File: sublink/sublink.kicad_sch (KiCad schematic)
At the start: 44 parts, among them J1 ZL315-4SGH, Q1 YJL2305A, SW1 SW_Push, SW2 SW_Push, SW3 SW_Push, U1 ATtiny414-SS, U2 OKY3402, U3 JS202011

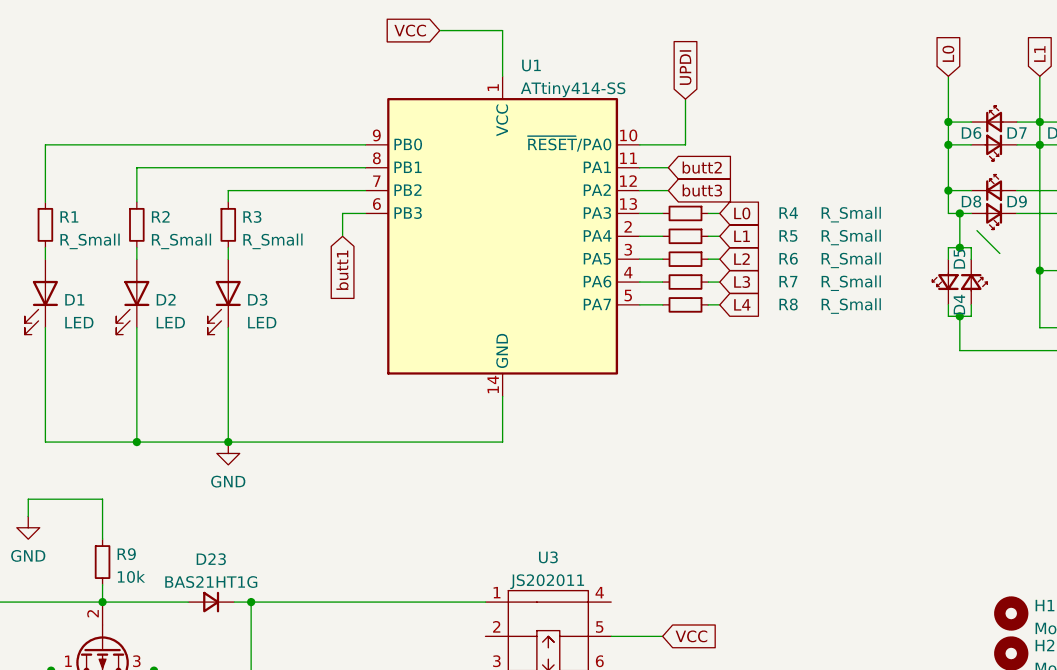
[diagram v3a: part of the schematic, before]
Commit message: first pass all components placement
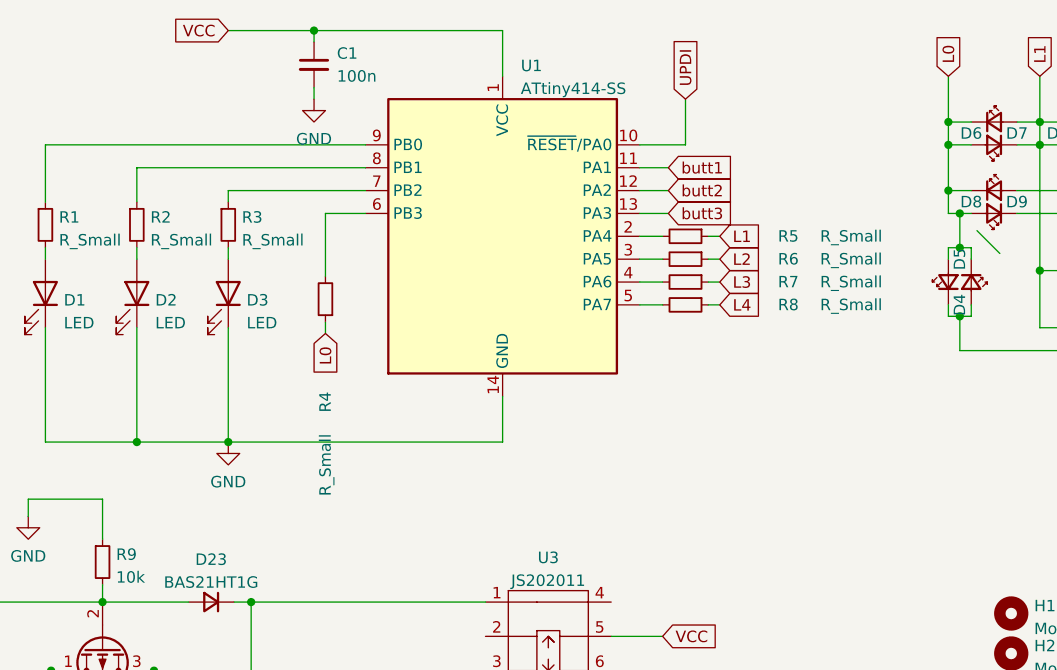
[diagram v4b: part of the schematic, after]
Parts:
- added C1: 100n, Capacitor_SMD:C_0805_2012Metric_Pad1.18x1.45mm_HandSolder, symbol Device:C_Small
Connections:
- net GND: now also C1.2
- net VCC: now also C1.1
- net butt1: now also U1.11 (PA1); no longer U1.6 (PB3)
- net butt2: now also U1.12 (PA2); no longer U1.11 (PA1)
- net butt3: now also U1.13 (PA3); no longer U1.12 (PA2)
- net at R4.2: now also U1.6 (PB3); no longer U1.13 (PA3)
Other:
- moved on the sheet: R4
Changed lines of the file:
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@@
   (junction (at 217.17 41.91) (diameter 0) (color 0 0 0 0)
   )
+  (junction (at 106.045 29.21) (diameter 0) (color 0 0 0 0)
+  )
   (junction (at 96.52 74.93) (diameter 0) (color 0 0 0 0)
   )
@@
     (stroke (width 0) (type default) (color 0 0 0 0))
   )
-  (wire (pts (xy 142.24 49.53) (xy 144.78 49.53))
-    (stroke (width 0) (type default) (color 0 0 0 0))
-  )
   (wire (pts (xy 207.01 39.37) (xy 207.01 34.29))
     (stroke (width 0) (type default) (color 0 0 0 0))
@@
     (stroke (width 0) (type default) (color 0 0 0 0))
   )
+  (wire (pts (xy 106.045 35.56) (xy 106.045 36.83))
+    (stroke (width 0) (type default) (color 0 0 0 0))
+  )
   (wire (pts (xy 184.15 39.37) (xy 186.69 39.37))
     (stroke (width 0) (type default) (color 0 0 0 0))
@@
     (stroke (width 0) (type default) (color 0 0 0 0))
   )
+  (wire (pts (xy 106.045 29.21) (xy 127 29.21))
+    (stroke (width 0) (type default) (color 0 0 0 0))
+  )
   (wire (pts (xy 142.24 59.69) (xy 144.78 59.69))
     (stroke (width 0) (type default) (color 0 0 0 0))
@@
     (stroke (width 0) (type default) (color 0 0 0 0))
   )
-  (wire (pts (xy 109.22 52.07) (xy 109.22 49.53))
-    (stroke (width 0) (type default) (color 0 0 0 0))
-  )
   (wire (pts (xy 82.55 81.28) (xy 74.295 81.28))
     (stroke (width 0) (type default) (color 0 0 0 0))
@@
     (stroke (width 0) (type default) (color 0 0 0 0))
   )
-  (wire (pts (xy 149.86 49.53) (xy 151.13 49.53))
+  (wire (pts (xy 107.315 61.595) (xy 107.315 62.865))
     (stroke (width 0) (type default) (color 0 0 0 0))
   )
@@
     (stroke (width 0) (type default) (color 0 0 0 0))
   )
+  (wire (pts (xy 142.24 49.53) (xy 145.415 49.53))
+    (stroke (width 0) (type default) (color 0 0 0 0))
+  )
   (wire (pts (xy 176.53 60.96) (xy 177.8 60.96))
     (stroke (width 0) (type default) (color 0 0 0 0))
@@
     (stroke (width 0) (type default) (color 0 0 0 0))
   )
-  (wire (pts (xy 109.22 49.53) (xy 111.76 49.53))
+  (wire (pts (xy 107.315 49.53) (xy 111.76 49.53))
     (stroke (width 0) (type default) (color 0 0 0 0))
   )
@@
     (stroke (width 0) (type default) (color 0 0 0 0))
   )
+  (wire (pts (xy 107.315 56.515) (xy 107.315 49.53))
+    (stroke (width 0) (type default) (color 0 0 0 0))
+  )
   (wire (pts (xy 177.8 53.34) (xy 179.07 53.34))
     (stroke (width 0) (type default) (color 0 0 0 0))
@@
     (stroke (width 0) (type default) (color 0 0 0 0))
   )
-  (wire (pts (xy 120.015 29.21) (xy 127 29.21))
+  (wire (pts (xy 96.52 29.21) (xy 106.045 29.21))
     (stroke (width 0) (type default) (color 0 0 0 0))
   )
@@
   )
   (wire (pts (xy 25.4 60.96) (xy 25.4 62.23))
+    (stroke (width 0) (type default) (color 0 0 0 0))
+  )
+  (wire (pts (xy 106.045 29.21) (xy 106.045 30.48))
     (stroke (width 0) (type default) (color 0 0 0 0))
   )
@@
     (effects (font (size 1.27 1.27)) (justify left bottom))
   )
-  (global_label "VCC" (shape input) (at 120.015 29.21 180) (fields_autoplaced)
+  (global_label "VCC" (shape input) (at 96.52 29.21 180) (fields_autoplaced)
     (effects (font (size 1.27 1.27)) (justify right))
-    (property "Intersheet References" "${INTERSHEET_REFS}" (id 0) (at 113.9733 29.2894 0)
-      (effects (font (size 1.27 1.27)) (justify right) hide)
-    )
-  )
-  (global_label "L0" (shape input) (at 151.13 49.53 0) (fields_autoplaced)
-    (effects (font (size 1.27 1.27)) (justify left))
-    (property "Intersheet References" "${INTERSHEET_REFS}" (id 0) (at 155.7807 49.4506 0)
-      (effects (font (size 1.27 1.27)) (justify left) hide)
+    (property "Intersheet References" "${INTERSHEET_REFS}" (id 0) (at 90.4783 29.2894 0)
+      (effects (font (size 1.27 1.27)) (justify right) hide)
+    )
+  )
+  (global_label "L0" (shape input) (at 107.315 62.865 270) (fields_autoplaced)
+    (effects (font (size 1.27 1.27)) (justify right))
+    (property "Intersheet References" "${INTERSHEET_REFS}" (id 0) (at 107.3944 67.5157 90)
+      (effects (font (size 1.27 1.27)) (justify right) hide)
     )
   )
@@
     )
   )
-  (global_label "butt3" (shape input) (at 145.415 46.99 0) (fields_autoplaced)
+  (global_label "butt2" (shape input) (at 145.415 46.99 0) (fields_autoplaced)
     (effects (font (size 1.27 1.27)) (justify left))
     (property "Intersheet References" "${INTERSHEET_REFS}" (id 0) (at 152.7871 46.9106 0)
@@
     )
   )
-  (global_label "butt2" (shape input) (at 145.415 44.45 0) (fields_autoplaced)
+  (global_label "butt1" (shape input) (at 145.415 44.45 0) (fields_autoplaced)
     (effects (font (size 1.27 1.27)) (justify left))
     (property "Intersheet References" "${INTERSHEET_REFS}" (id 0) (at 152.7871 44.3706 0)
@@
     )
   )
-  (global_label "butt1" (shape input) (at 109.22 52.07 270) (fields_autoplaced)
-    (effects (font (size 1.27 1.27)) (justify right))
-    (property "Intersheet References" "${INTERSHEET_REFS}" (id 0) (at 109.1406 59.4421 90)
-      (effects (font (size 1.27 1.27)) (justify right) hide)
+  (global_label "butt3" (shape input) (at 145.415 49.53 0) (fields_autoplaced)
+    (effects (font (size 1.27 1.27)) (justify left))
+    (property "Intersheet References" "${INTERSHEET_REFS}" (id 0) (at 152.7871 49.4506 0)
+      (effects (font (size 1.27 1.27)) (justify left) hide)
     )
   )
@@
     (pin "4")
   )
-  (symbol (lib_id "Device:R_Small") (at 147.32 49.53 270) (unit 1)
-    (in_bom yes) (on_board yes)
-    (property "Reference" "R4" (id 0) (at 158.75 49.53 90))
-    (property "Value" "R_Small" (id 1) (at 165.735 49.53 90))
-    (property "Footprint" "Resistor_SMD:R_0805_2012Metric_Pad1.20x1.40mm_HandSolder" (id 2) (at 147.32 49.53 0)
-      (effects (font (size 1.27 1.27)) hide)
-    )
-    (property "Datasheet" "~" (id 3) (at 147.32 49.53 0)
+  (symbol (lib_id "Device:R_Small") (at 107.315 59.055 180) (unit 1)
+    (in_bom yes) (on_board yes)
+    (property "Reference" "R4" (id 0) (at 107.315 70.485 90))
+    (property "Value" "R_Small" (id 1) (at 107.315 77.47 90))
+    (property "Footprint" "Resistor_SMD:R_0805_2012Metric_Pad1.20x1.40mm_HandSolder" (id 2) (at 107.315 59.055 0)
+      (effects (font (size 1.27 1.27)) hide)
+    )
+    (property "Datasheet" "~" (id 3) (at 107.315 59.055 0)
       (effects (font (size 1.27 1.27)) hide)
     )
@@
     )
     (pin "1")
+  )
+  (symbol (lib_id "Device:C_Small") (at 106.045 33.02 0) (unit 1)
+    (in_bom yes) (on_board yes) (fields_autoplaced)
+    (property "Reference" "C1" (id 0) (at 108.585 31.7562 0)
+      (effects (font (size 1.27 1.27)) (justify left))
+    )
+    (property "Value" "100n" (id 1) (at 108.585 34.2962 0)
+      (effects (font (size 1.27 1.27)) (justify left))
+    )
+    (property "Footprint" "Capacitor_SMD:C_0805_2012Metric_Pad1.18x1.45mm_HandSolder" (id 2) (at 106.045 33.02 0)
+      (effects (font (size 1.27 1.27)) hide)
+    )
+    (property "Datasheet" "~" (id 3) (at 106.045 33.02 0)
+      (effects (font (size 1.27 1.27)) hide)
+    )
+    (pin "1")
+    (pin "2")
   )
   (symbol (lib_id "Switch:SW_Push") (at 48.26 55.88 90) (unit 1)
@@
     (pin "1")
     (pin "2")
+  )
+  (symbol (lib_id "power:GND") (at 106.045 36.83 0) (unit 1)
+    (in_bom yes) (on_board yes) (fields_autoplaced)
+    (property "Reference" "#PWR0106" (id 0) (at 106.045 43.18 0)
+      (effects (font (size 1.27 1.27)) hide)
+    )
+    (property "Value" "GND" (id 1) (at 106.045 41.2734 0))
+    (property "Footprint" "" (id 2) (at 106.045 36.83 0)
+      (effects (font (size 1.27 1.27)) hide)
+    )
+    (property "Datasheet" "" (id 3) (at 106.045 36.83 0)
+      (effects (font (size 1.27 1.27)) hide)
+    )
+    (pin "1")
   )
   (symbol (lib_id "power:GND") (at 96.52 74.93 0) (unit 1)
@@
       (reference "#PWR0105") (unit 1) (value "GND") (footprint "")
     )
+    (path "/c5208e41-cdca-42ff-913f-4cf604cda756"
+      (reference "#PWR0106") (unit 1) (value "GND") (footprint "")
+    )
     (path "/49787c66-f49d-4a79-a51d-f0e535a60cc0"
       (reference "BT1") (unit 1) (value "3V7") (footprint "Connector_PinHeader_2.54mm:PinHeader_1x02_P2.54mm_Vertical")
     )
+    (path "/8a653a42-4334-4d27-9c26-7376a1c6c756"
+      (reference "C1") (unit 1) (value "100n") (footprint "Capacitor_SMD:C_0805_2012Metric_Pad1.18x1.45mm_HandSolder")
+    )
     (path "/57d2df35-9220-4089-b425-124a7c59e2d6"

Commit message: wip routing
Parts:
- removed Q1: YJL2305A, Package_TO_SOT_SMD:SOT-23, symbol Device:Q_PMOS_DGS
- added Q1: Q_PMOS_GSD, Package_TO_SOT_SMD:SOT-23, symbol Device:Q_PMOS_GSD
- BT1: footprint Connector_PinHeader_2.54mm:PinHeader_1x02_P2.54mm_Vertical -> Resistor_SMD:R_1206_3216Metric_Pad1.30x1.75mm_HandSolder
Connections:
- net VCC: now also U3.2
- net at D23.2 (A), R9.2, U2.2 (USB+): now also Q1.1 (G)
- net at BT1.1 (+), D22.2 (A), U2.4 (B+): now also Q1.3 (D)
- net at D22.1 (K), D23.1 (K): now also U3.6, Q1.2 (S); no longer U3.1
- net at J1.1 (Pin_1): now also U3.1; no longer U3.3
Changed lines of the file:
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@@
   (junction (at 62.865 114.935) (diameter 0) (color 0 0 0 0)
   )
+  (junction (at 196.85 49.53) (diameter 0) (color 0 0 0 0)
+  )
   (junction (at 99.06 92.71) (diameter 0) (color 0 0 0 0)
   )
-  (junction (at 196.85 49.53) (diameter 0) (color 0 0 0 0)
-  )
   (junction (at 217.17 46.99) (diameter 0) (color 0 0 0 0)
   )
@@
     (stroke (width 0) (type default) (color 0 0 0 0))
   )
+  (wire (pts (xy 121.285 96.52) (xy 125.095 96.52))
+    (stroke (width 0) (type default) (color 0 0 0 0))
+  )
   (wire (pts (xy 62.865 114.935) (xy 69.215 114.935))
     (stroke (width 0) (type default) (color 0 0 0 0))
@@
     (stroke (width 0) (type default) (color 0 0 0 0))
   )
-  (wire (pts (xy 120.015 115.57) (xy 120.015 100.33))
-    (stroke (width 0) (type default) (color 0 0 0 0))
-  )
   (wire (pts (xy 86.36 62.23) (xy 86.36 74.93))
     (stroke (width 0) (type default) (color 0 0 0 0))
@@
     (stroke (width 0) (type default) (color 0 0 0 0))
   )
+  (wire (pts (xy 116.205 92.71) (xy 99.06 92.71))
+    (stroke (width 0) (type default) (color 0 0 0 0))
+  )
   (wire (pts (xy 207.01 41.91) (xy 207.01 55.88))
     (stroke (width 0) (type default) (color 0 0 0 0))
@@
     (stroke (width 0) (type default) (color 0 0 0 0))
   )
+  (wire (pts (xy 120.015 92.71) (xy 120.015 115.57))
+    (stroke (width 0) (type default) (color 0 0 0 0))
+  )
   (wire (pts (xy 214.63 46.99) (xy 217.17 46.99))
     (stroke (width 0) (type default) (color 0 0 0 0))
@@
     (stroke (width 0) (type default) (color 0 0 0 0))
   )
-  (wire (pts (xy 120.015 100.33) (xy 125.095 100.33))
-    (stroke (width 0) (type default) (color 0 0 0 0))
-  )
   (wire (pts (xy 217.17 39.37) (xy 217.17 41.91))
     (stroke (width 0) (type default) (color 0 0 0 0))
@@
     (stroke (width 0) (type default) (color 0 0 0 0))
   )
-  (wire (pts (xy 99.06 92.71) (xy 125.095 92.71))
+  (wire (pts (xy 116.205 82.55) (xy 116.205 92.71))
     (stroke (width 0) (type default) (color 0 0 0 0))
   )
@@
     (stroke (width 0) (type default) (color 0 0 0 0))
   )
+  (wire (pts (xy 142.875 82.55) (xy 116.205 82.55))
+    (stroke (width 0) (type default) (color 0 0 0 0))
+  )
   (wire (pts (xy 96.52 48.26) (xy 96.52 46.99))
     (stroke (width 0) (type default) (color 0 0 0 0))
@@
     (stroke (width 0) (type default) (color 0 0 0 0))
   )
-  (wire (pts (xy 139.065 96.52) (xy 144.78 96.52))
+  (wire (pts (xy 139.065 96.52) (xy 146.05 96.52))
     (stroke (width 0) (type default) (color 0 0 0 0))
   )
@@
     (stroke (width 0) (type default) (color 0 0 0 0))
   )
+  (wire (pts (xy 139.065 100.33) (xy 142.875 100.33))
+    (stroke (width 0) (type default) (color 0 0 0 0))
+  )
   (wire (pts (xy 186.69 55.88) (xy 193.04 55.88))
     (stroke (width 0) (type default) (color 0 0 0 0))
@@
     (stroke (width 0) (type default) (color 0 0 0 0))
   )
+  (wire (pts (xy 120.015 92.71) (xy 125.095 92.71))
+    (stroke (width 0) (type default) (color 0 0 0 0))
+  )
   (wire (pts (xy 214.63 41.91) (xy 217.17 41.91))
     (stroke (width 0) (type default) (color 0 0 0 0))
@@
   )
   (wire (pts (xy 176.53 39.37) (xy 179.07 39.37))
+    (stroke (width 0) (type default) (color 0 0 0 0))
+  )
+  (wire (pts (xy 142.875 82.55) (xy 142.875 100.33))
     (stroke (width 0) (type default) (color 0 0 0 0))
   )
@@
     )
   )
-  (global_label "VCC" (shape input) (at 144.78 96.52 0) (fields_autoplaced)
-    (effects (font (size 1.27 1.27)) (justify left))
-    (property "Intersheet References" "${INTERSHEET_REFS}" (id 0) (at 150.8217 96.4406 0)
+  (global_label "VCC" (shape input) (at 146.05 96.52 0) (fields_autoplaced)
+    (effects (font (size 1.27 1.27)) (justify left))
+    (property "Intersheet References" "${INTERSHEET_REFS}" (id 0) (at 152.0917 96.4406 0)
       (effects (font (size 1.27 1.27)) (justify left) hide)
     )
@@
     (property "Intersheet References" "${INTERSHEET_REFS}" (id 0) (at 126.9033 118.0306 0)
       (effects (font (size 1.27 1.27)) (justify left) hide)
+    )
+  )
+  (global_label "VCC" (shape input) (at 121.285 96.52 180) (fields_autoplaced)
+    (effects (font (size 1.27 1.27)) (justify right))
+    (property "Intersheet References" "${INTERSHEET_REFS}" (id 0) (at 115.2433 96.5994 0)
+      (effects (font (size 1.27 1.27)) (justify right) hide)
     )
   )
@@
       (effects (font (size 1.27 1.27)) (justify left))
     )
-    (property "Footprint" "Connector_PinHeader_2.54mm:PinHeader_1x02_P2.54mm_Vertical" (id 2) (at 69.215 105.791 90)
+    (property "Footprint" "Resistor_SMD:R_1206_3216Metric_Pad1.30x1.75mm_HandSolder" (id 2) (at 69.215 105.791 90)
       (effects (font (size 1.27 1.27)) hide)
     )
@@
     (pin "2")
   )
-  (symbol (lib_id "Device:Q_PMOS_DGS") (at 82.55 97.79 90) (mirror x) (unit 1)
-    (in_bom yes) (on_board yes)
-    (property "Reference" "Q1" (id 0) (at 82.55 103.505 90))
-    (property "Value" "YJL2305A" (id 1) (at 82.55 106.045 90))
+  (symbol (lib_id "Device:R_Small") (at 96.52 50.8 0) (unit 1)
+    (in_bom yes) (on_board yes) (fields_autoplaced)
+    (property "Reference" "R3" (id 0) (at 98.0186 49.9653 0)
+      (effects (font (size 1.27 1.27)) (justify left))
+    )
+    (property "Value" "R_Small" (id 1) (at 98.0186 52.5022 0)
+      (effects (font (size 1.27 1.27)) (justify left))
+    )
+    (property "Footprint" "Resistor_SMD:R_0805_2012Metric_Pad1.20x1.40mm_HandSolder" (id 2) (at 96.52 50.8 0)
+      (effects (font (size 1.27 1.27)) hide)
+    )
+    (property "Datasheet" "~" (id 3) (at 96.52 50.8 0)
+      (effects (font (size 1.27 1.27)) hide)
+    )
+    (pin "1")
+    (pin "2")
+  )
+  (symbol (lib_id "Device:Q_PMOS_GSD") (at 82.55 97.79 90) (mirror x) (unit 1)
+    (in_bom yes) (on_board yes) (fields_autoplaced)
+    (property "Reference" "Q1" (id 0) (at 82.55 104.2654 90))
+    (property "Value" "Q_PMOS_GSD" (id 1) (at 82.55 106.8023 90))
     (property "Footprint" "Package_TO_SOT_SMD:SOT-23" (id 2) (at 80.01 102.87 0)
       (effects (font (size 1.27 1.27)) hide)
@@
     (pin "2")
     (pin "3")
-  )
-  (symbol (lib_id "Device:R_Small") (at 96.52 50.8 0) (unit 1)
-    (in_bom yes) (on_board yes) (fields_autoplaced)
-    (property "Reference" "R3" (id 0) (at 98.0186 49.9653 0)
-      (effects (font (size 1.27 1.27)) (justify left))
-    )
-    (property "Value" "R_Small" (id 1) (at 98.0186 52.5022 0)
-      (effects (font (size 1.27 1.27)) (justify left))
-    )
-    (property "Footprint" "Resistor_SMD:R_0805_2012Metric_Pad1.20x1.40mm_HandSolder" (id 2) (at 96.52 50.8 0)
-      (effects (font (size 1.27 1.27)) hide)
-    )
-    (property "Datasheet" "~" (id 3) (at 96.52 50.8 0)
-      (effects (font (size 1.27 1.27)) hide)
-    )
-    (pin "1")
-    (pin "2")
   )
   (symbol (lib_id "Device:LED_Small") (at 212.09 41.91 180) (unit 1)
@@
     )
     (path "/49787c66-f49d-4a79-a51d-f0e535a60cc0"
-      (reference "BT1") (unit 1) (value "3V7") (footprint "Connector_PinHeader_2.54mm:PinHeader_1x02_P2.54mm_Vertical")
+      (reference "BT1") (unit 1) (value "3V7") (footprint "Resistor_SMD:R_1206_3216Metric_Pad1.30x1.75mm_HandSolder")
     )
     (path "/8a653a42-4334-4d27-9c26-7376a1c6c756"
@@
       (reference "J1") (unit 1) (value "ZL315-4SGH") (footprint "Connector_Harwin:Harwin_M20-89004xx_1x04_P2.54mm_Horizontal")
     )
-    (path "/aa0a099c-479d-4909-8f65-0af88e650102"
-      (reference "Q1") (unit 1) (value "YJL2305A") (footprint "Package_TO_SOT_SMD:SOT-23")
+    (path "/aef741e9-e229-4c8d-b8c3-21ad5f571a00"
+      (reference "Q1") (unit 1) (value "Q_PMOS_GSD") (footprint "Package_TO_SOT_SMD:SOT-23")
     )
     (path "/480cfc26-2c62-4bd8-bba1-ebc5c356850c"

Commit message: wip top radial routing
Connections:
- net at U3.1: no longer J1.1 (Pin_1)
- net at U3.3: now also J1.1 (Pin_1)
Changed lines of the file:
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@@
+    (stroke (width 0) (type default) (color 0 0 0 0))
+  )
+  (wire (pts (xy 120.015 115.57) (xy 120.015 100.33))
     (stroke (width 0) (type default) (color 0 0 0 0))
   )
@@
     (stroke (width 0) (type default) (color 0 0 0 0))
   )
-  (wire (pts (xy 120.015 92.71) (xy 120.015 115.57))
-    (stroke (width 0) (type default) (color 0 0 0 0))
-  )
   (wire (pts (xy 214.63 46.99) (xy 217.17 46.99))
     (stroke (width 0) (type default) (color 0 0 0 0))
@@
     (stroke (width 0) (type default) (color 0 0 0 0))
   )
+  (wire (pts (xy 120.015 100.33) (xy 125.095 100.33))
+    (stroke (width 0) (type default) (color 0 0 0 0))
+  )
   (wire (pts (xy 116.205 82.55) (xy 116.205 92.71))
     (stroke (width 0) (type default) (color 0 0 0 0))
@@
     (stroke (width 0) (type default) (color 0 0 0 0))
   )
-  (wire (pts (xy 120.015 92.71) (xy 125.095 92.71))
-    (stroke (width 0) (type default) (color 0 0 0 0))
-  )
